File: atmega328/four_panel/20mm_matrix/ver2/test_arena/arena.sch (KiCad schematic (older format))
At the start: 35 parts, among them P1 CONN15, P10 CONN_2X2, P11 CONN_2X2, P12 CONN_2X2, P13 CONN_2X2, P14 CONN_2X2, P15 CONN_2X2, P16 CONN_2X2, P17 CONN_2X2, P18 CONN_2X2, P19 CONN_2X2, P2 CONN15, P20 CONN_2X2, P21 CONN_2X2, P22 CONN_20X2, P23 CONN_30X2, P24 CONN_2, P25 CONN_5X2, P26 CONN_5X2, P27 CONN_5X2, P28 CONN_5X2, P29 CONN_5X2, P3 CONN15, P30 CONN_20X2, P4 CONN15, P5 CONN15, P6 CONN15, P7 CONN_2X2, P8 CONN_2X2, P9 CONN_2X2

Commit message: Finished new test arena design - for atmega328 4x20mm panels v0.2
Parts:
- removed P10, P11, P12, P13, P14, P15, P16, P17, P18, P19, P20, P21, P7, P8, P9: CONN_2X2, symbol CONN_2X2
- removed P23: CONN_30X2, symbol CONN_30X2
- removed P25, P26, P27, P28, P29: CONN_5X2, symbol CONN_5X2
- removed P30: CONN_20X2, symbol CONN_20X2
- added P8: CONN_34X2, symbol CONN_34X2
- added SW1: SWITCH_INV, symbol SWITCH_INV
- renumbered P22 to P7, P24 to P9
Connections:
- net labels added: CS0, CS1, CS2, CS3, CS4, CS5, CS6, CS7, EXT_INT, RESET, VIN
- net labels removed: CS1_0, CS1_1, CS1_2, CS1_3, CS1_4, CS1_5, CS2_0, CS2_1, CS2_2, CS2_3, CS2_4, CS2_5, CS3_0, CS3_1, CS3_2, CS3_3, CS3_4, CS3_5, CS4_0, CS4_1, CS4_2, CS4_3, CS4_4, CS4_5, CS5_0, CS5_1, CS5_2, CS5_3, CS5_4, CS5_5, EXT_INT0, EXT_INT1, MISO_11, MISO_22, MISO_33, MISO_44, MISO_55, MOSI_11, MOSI_22, MOSI_33, MOSI_44, MOSI_55, RESET_MSTR, RX, SCK_11, SCK_22, SCK_33, SCK_44, SCK_55, TX
- wire segments 386 -> 188
- no-connect marks 11 -> 47
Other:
- note added: "68-pin DSUB for NI cable, TE Connectivity 2-5174225-5\nDigikey PN A33476-ND"
- note removed: "30x2 Header (Digikey HRU60H-ND), IDC Cable (Digkey HKC60S-ND)"
- note removed: "Bus Selectors"
- moved on the sheet: C1, C2, C3, C4, C5, P7, P9

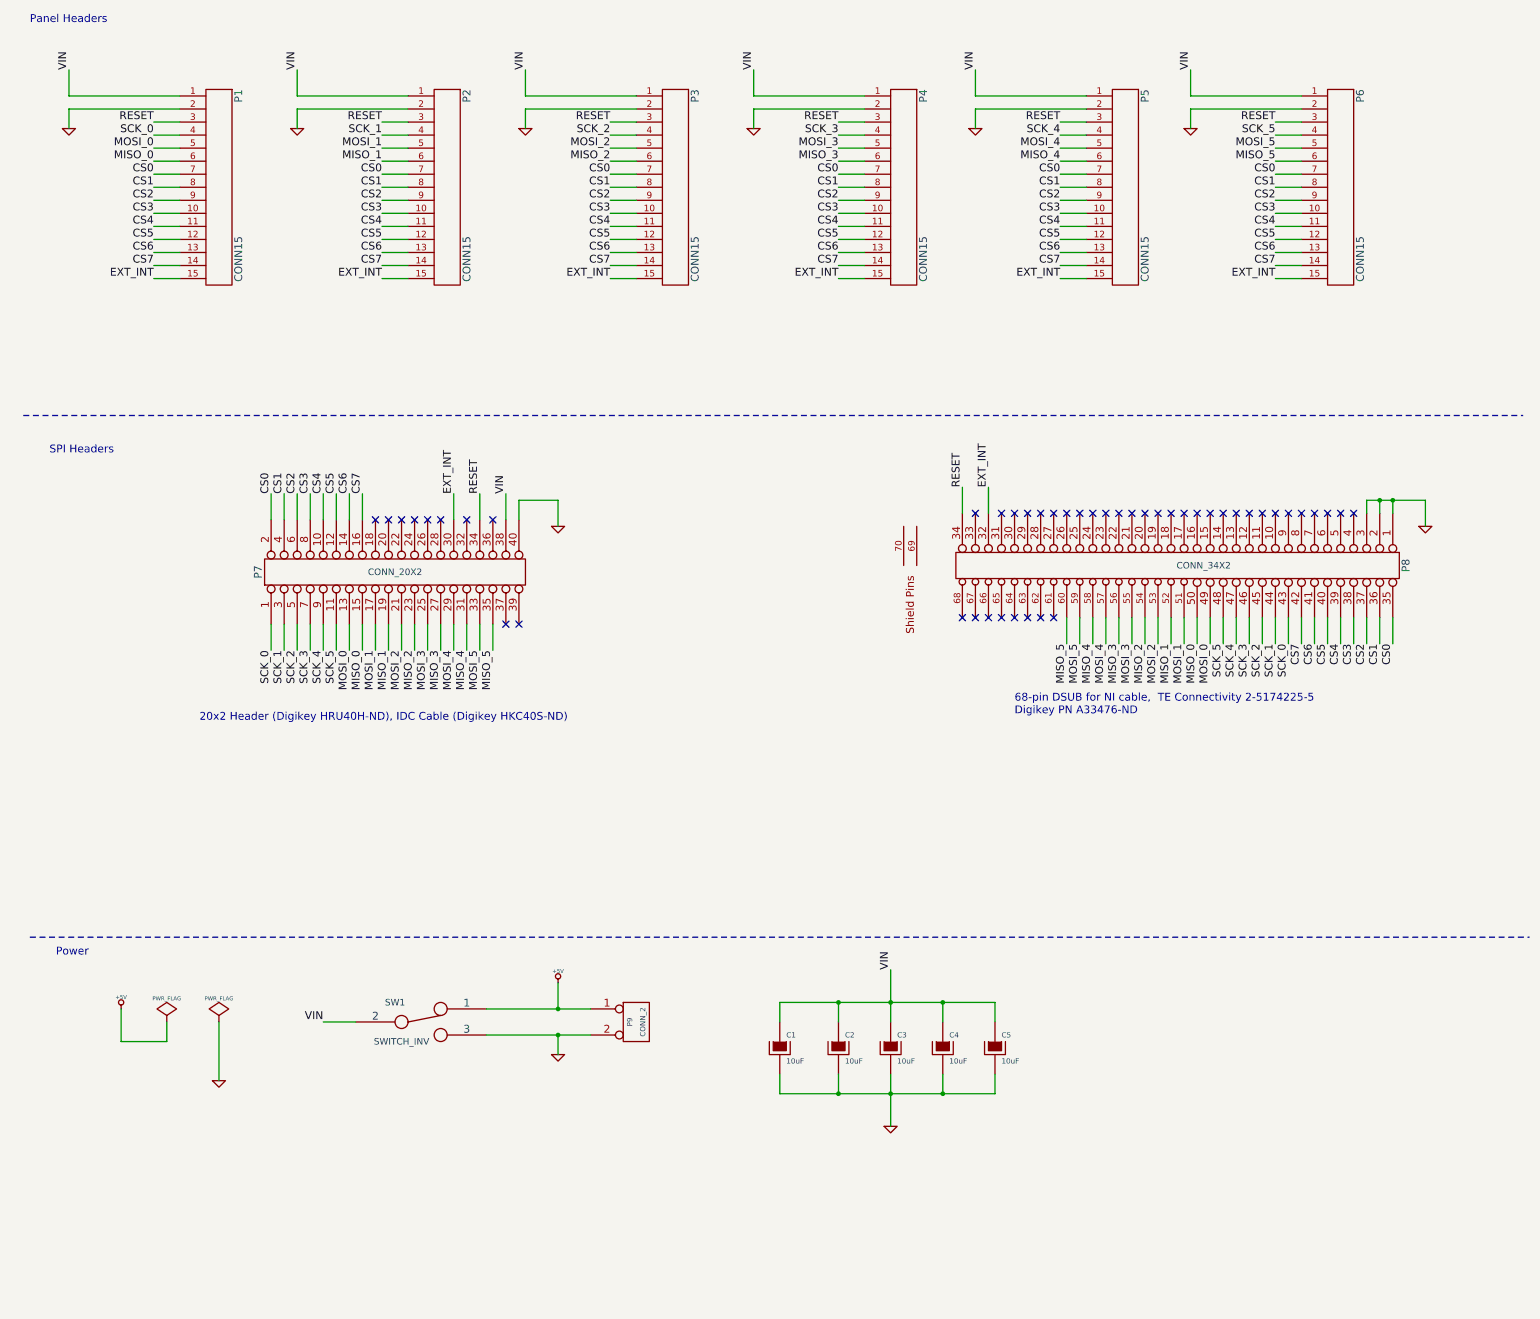
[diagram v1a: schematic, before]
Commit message: Worked on v0.2 test arena for atmega328 4x20mm panels. Added mosfet switch for reset. Modified for chaining via the 20x2 header so that we can drive 12 columns of panels.
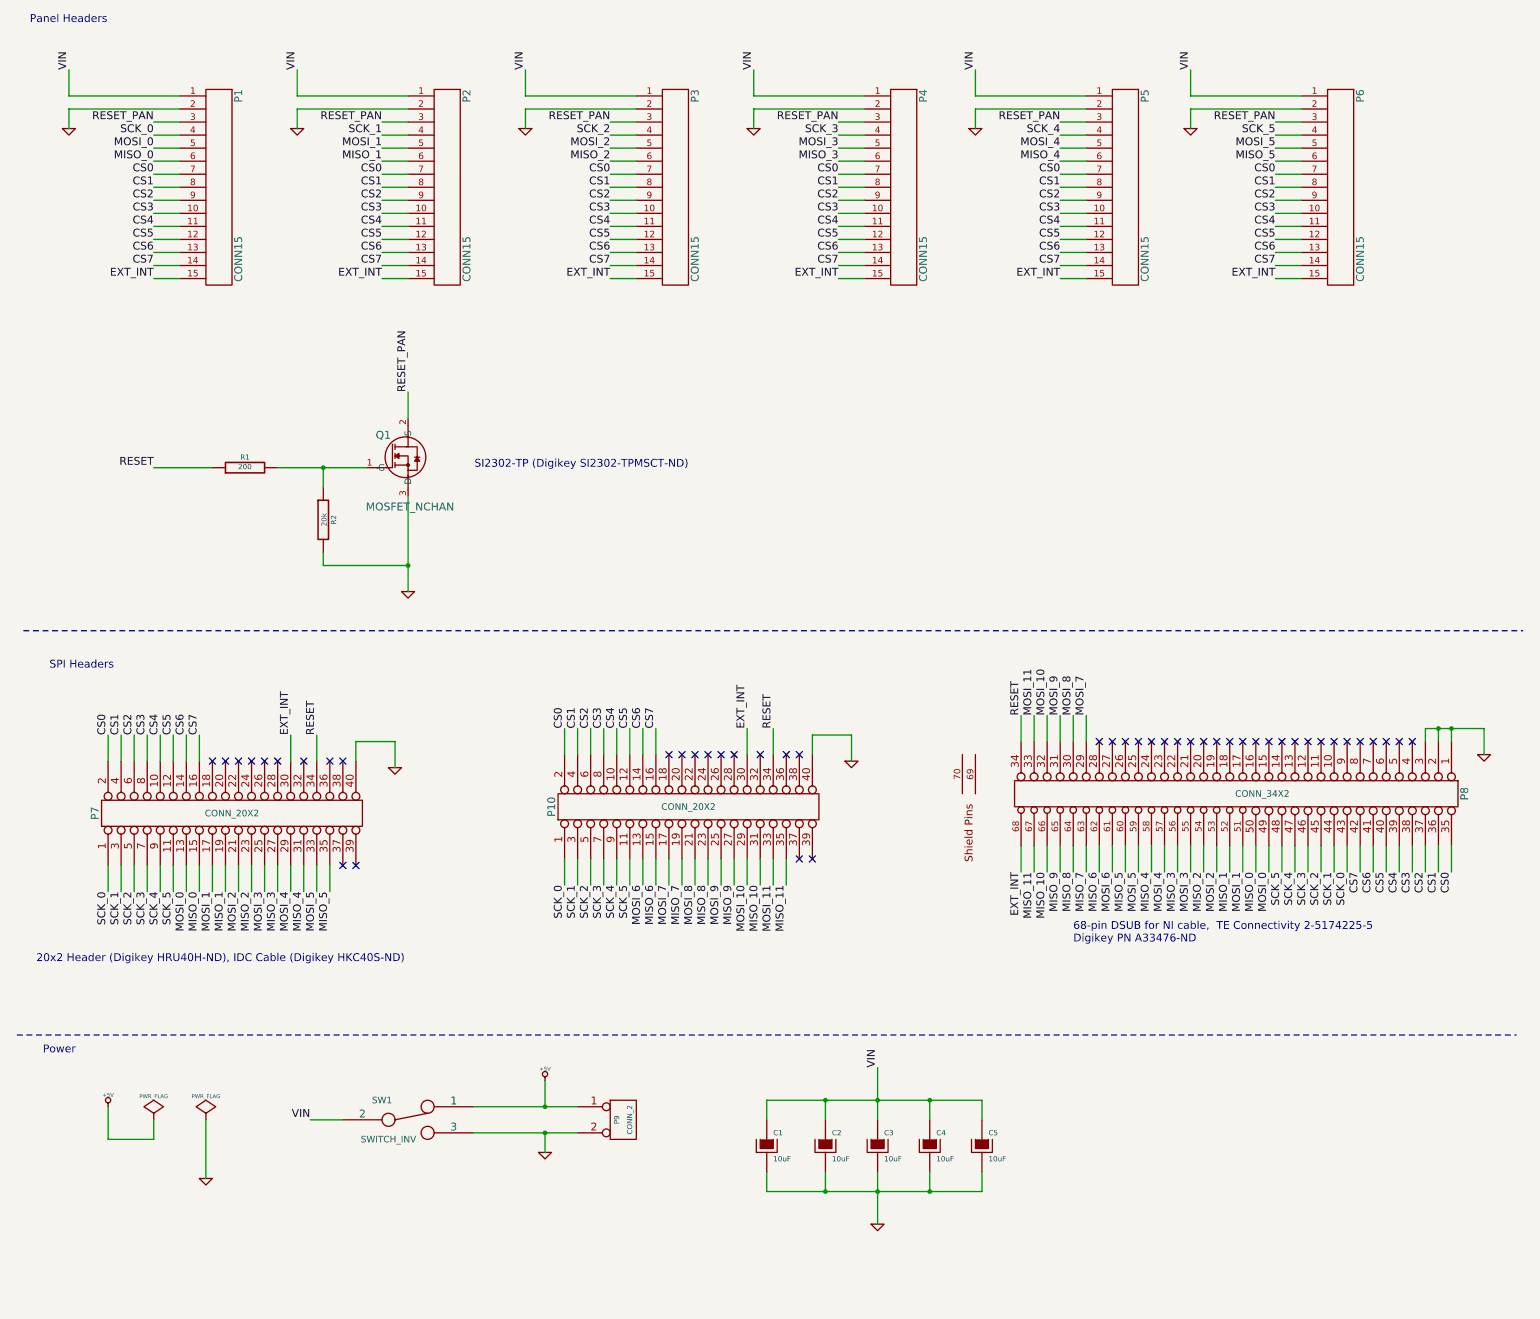
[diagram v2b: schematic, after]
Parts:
- added P10: CONN_20X2, symbol CONN_20X2
- added Q1: MOSFET_NCHAN, symbol MOSFET_NCHAN
- added R1: 200, symbol R
- added R2: 20k, symbol R
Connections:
- net CS0: now also P10.2 (P2)
- net CS1: now also P10.4 (P4)
- net CS2: now also P10.6 (P6)
- net CS3: now also P10.8 (P8)
- net CS4: now also P10.10 (P10)
- net CS5: now also P10.12 (P12)
- net CS6: now also P10.14 (P14)
- net CS7: now also P10.16 (P16)
- net EXT_INT: now also P8.68, P10.30 (P30); no longer P8.32 (P32)
- net GND: now also P10.40 (P40), Q1.3 (D), R2.2
- net RESET: now also P10.34 (P34), R1.1; no longer P1.3, P2.3, P3.3, P4.3, P5.3, P6.3
- net SCK_0: now also P10.1 (P1)
- net SCK_1: now also P10.3 (P3)
- net SCK_2: now also P10.5 (P5)
- net SCK_3: now also P10.7 (P7)
- net SCK_4: now also P10.9 (P9)
- net SCK_5: now also P10.11 (P11)
- net VIN: no longer P7.38 (P38)
- net MOSI_7: now reaches P8.29 (P29)
- net MOSI_7: now also P10.17 (P17)
- net MOSI_8: now reaches P8.30 (P30)
- net MOSI_8: now also P10.21 (P21)
- net MOSI_9: now reaches P8.31 (P31)
- net MOSI_9: now also P10.25
- net MOSI_11: now reaches P8.33 (P33)
- net MOSI_11: now also P10.33 (P33)
- net MOSI_6: now reaches P8.61
- net MOSI_6: now also P10.13 (P13)
- net MISO_6: now reaches P8.62
- net MISO_6: now also P10.15 (P15)
- net MISO_7: now reaches P8.63
- net MISO_7: now also P10.19 (P19)
- net MISO_8: now reaches P8.64
- net MISO_8: now also P10.23 (P23)
- net MISO_9: now reaches P8.65
- net MISO_9: now also P10.27 (P27)
- net MISO_10: now reaches P8.66
- net MISO_10: now also P10.31 (P31)
- net MISO_11: now reaches P8.67
- net MISO_11: now also P10.35 (P35)
- new net: Q1.1 (G), R1.2, R2.1
- new net MOSI_10: P10.29 (P29), P8.32 (P32)
- new net RESET_PAN: P1.3, P2.3, P3.3, P4.3, P5.3, P6.3, Q1.2 (S)
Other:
- note added: "SI2302-TP (Digikey SI2302-TPMSCT-ND)"
- moved on the sheet: C1, C2, C3, C4, C5, P7, P8, P9, SW1

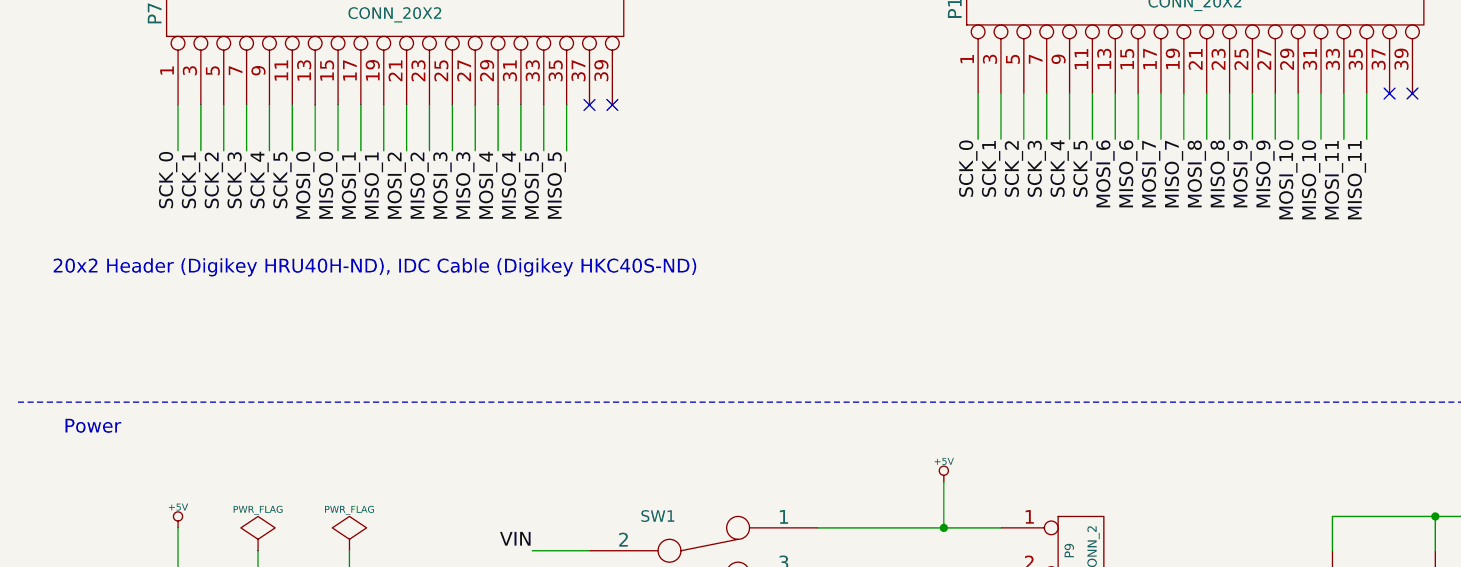
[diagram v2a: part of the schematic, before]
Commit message: Modified pwr,gnd and reset_pan trace widths. Re-routed.
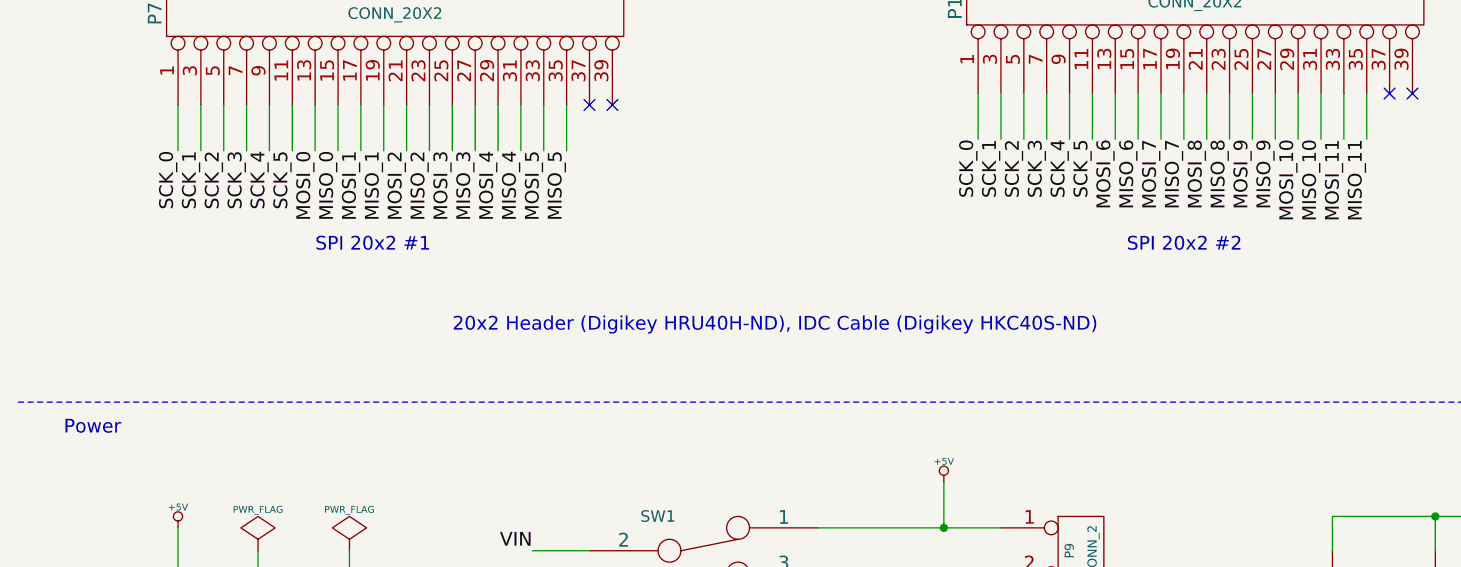
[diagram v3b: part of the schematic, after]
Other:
- note added: "SPI 20x2 #1"
- note added: "SPI 20x2 #2"
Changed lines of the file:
@@
 NoConn ~ 2950 7100
 NoConn ~ 3050 7100
-Text Notes 600  7850 0    60   ~ 0
+Text Notes 2350 8100 0    60   ~ 0
 20x2 Header (Digikey HRU40H-ND), IDC Cable (Digikey HKC40S-ND)
 Text Notes 8550 7700 0    60   ~ 0
@@
 Wire Wire Line
 	3450 3675 3450 3470
+Text Notes 1750 7750 0    60   ~ 0
+SPI 20x2 #1
+Text Notes 5300 7750 0    60   ~ 0
+SPI 20x2 #2
 $EndSCHEMATC

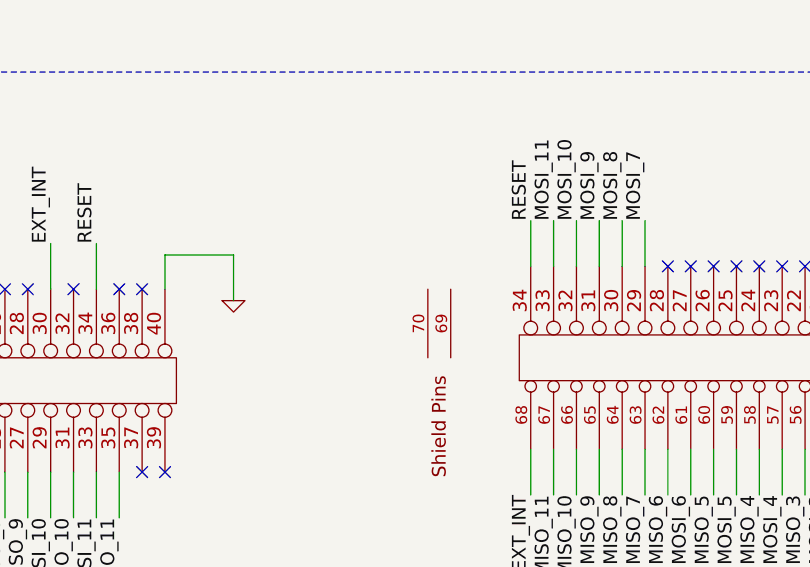
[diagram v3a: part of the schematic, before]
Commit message: Added gerber files for new arena design.
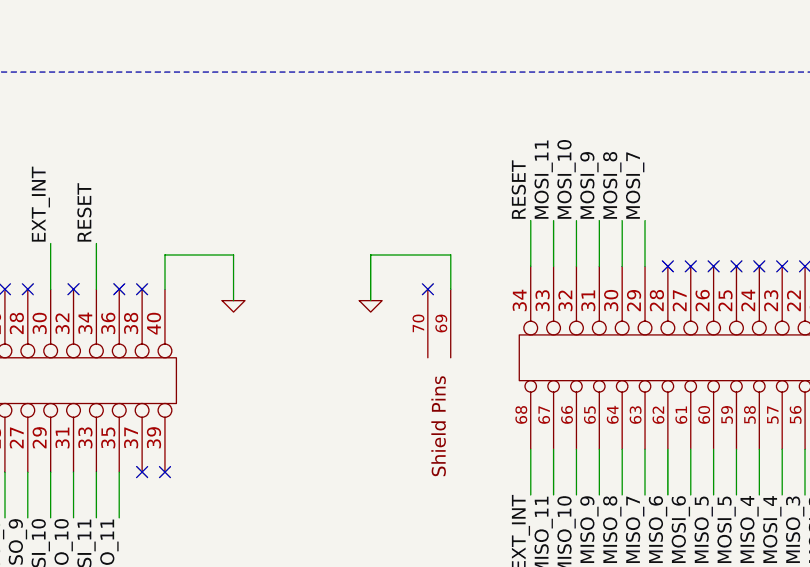
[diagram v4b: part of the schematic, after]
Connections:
- net GND: now also P8.69
- no-connect marks 47 -> 48
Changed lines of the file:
@@
 Text Notes 5300 7750 0    60   ~ 0
 SPI 20x2 #2
+Wire Wire Line
+	7800 6100 7800 6250
+Wire Wire Line
+	7450 6100 7800 6100
+Wire Wire Line
+	7450 6100 7450 6300
+$Comp
+L GND #PWR018
+U 1 1 5435D913
+P 7450 6300
+F 0 "#PWR018" H 7450 6300 30  0001 C CNN
+F 1 "GND" H 7450 6230 30  0001 C CNN
+F 2 "" H 7450 6300 60  0000 C CNN
+F 3 "" H 7450 6300 60  0000 C CNN
+	1    7450 6300
+	1    0    0    -1
+$EndComp
+NoConn ~ 7700 6250
 $EndSCHEMATC

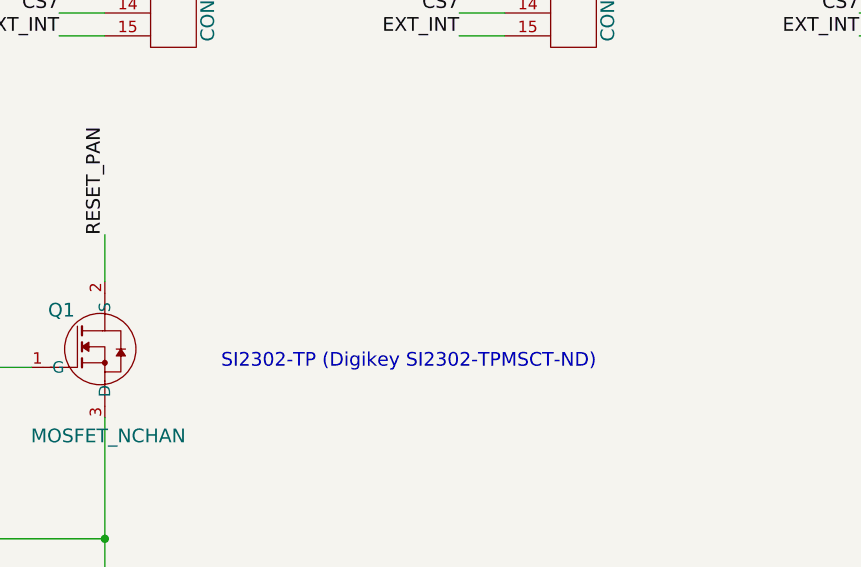
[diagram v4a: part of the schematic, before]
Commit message: Added note about error in reset MOSFET circuit on test arena.
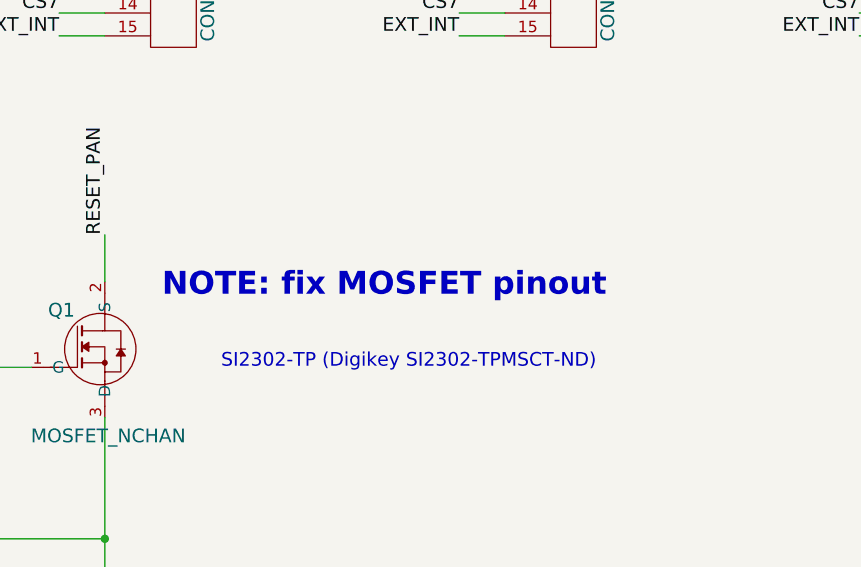
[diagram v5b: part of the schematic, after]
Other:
- note added: "NOTE: fix MOSFET pinout"
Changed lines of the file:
@@
 $EndComp
 NoConn ~ 7700 6250
+Text Notes 3700 3750 0    100  ~ 20
+NOTE: fix MOSFET pinout
 $EndSCHEMATC
